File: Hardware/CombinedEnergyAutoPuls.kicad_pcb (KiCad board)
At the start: 2 copper layers, 174.9 x 67 mm, 131 parts, among them J1 Screw_Terminal_01x04, J101 AudioJack3_Switch, J102 Screw_Terminal_01x03, J103 Conn_3P, J2 Screw_Terminal_01x04, J201 Conn_20P_Female, J202 Conn_20P_Female, J203 Conn_4P_Female, J204 Conn_4P_Female, J205 Barrel_Jack_Switch, J3 Pin_Header_1x6, J4 Arduino_USB-Serial_Card_Conne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, J5 Arduino_USB-Serial_Edge_Conne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, J6 AudioJack3_Switch, J7 Screw_Terminal_01x04, Q1 S8550_PNP, Q101 S8050_NPN, Q2 S8050_NPN, Q3 S8050_NPN, SW201 THT_SW_4_Tactile, U1 L78S05CV, U101 LM358DR2G, U102 78L05, U201 PC817, U202 PC817, U203 PC817, U204 PC817, U205 PC817, U206 PC817, U207 PC817, U208 PC817, U209 PC817, U210 PC817, U211 PC817, U212 L78S05CV

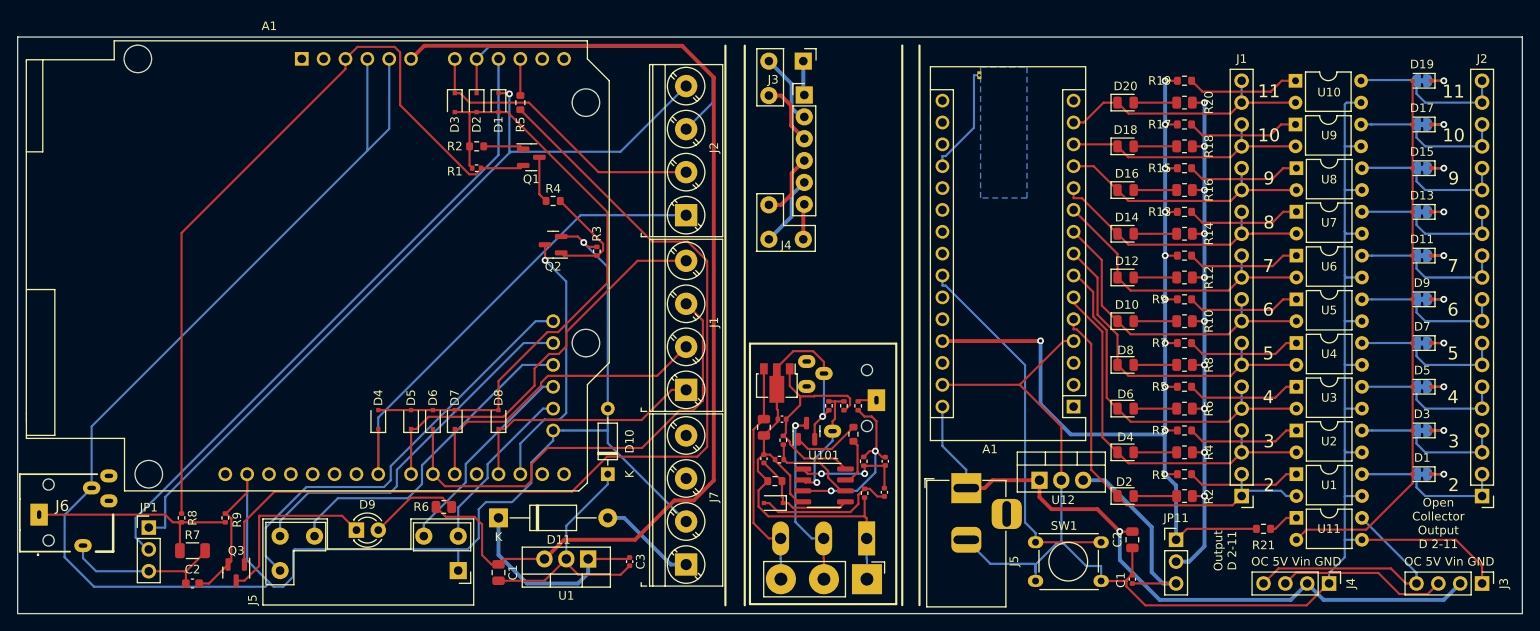
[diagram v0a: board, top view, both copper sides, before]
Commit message: GND zone filled for Energimaaling
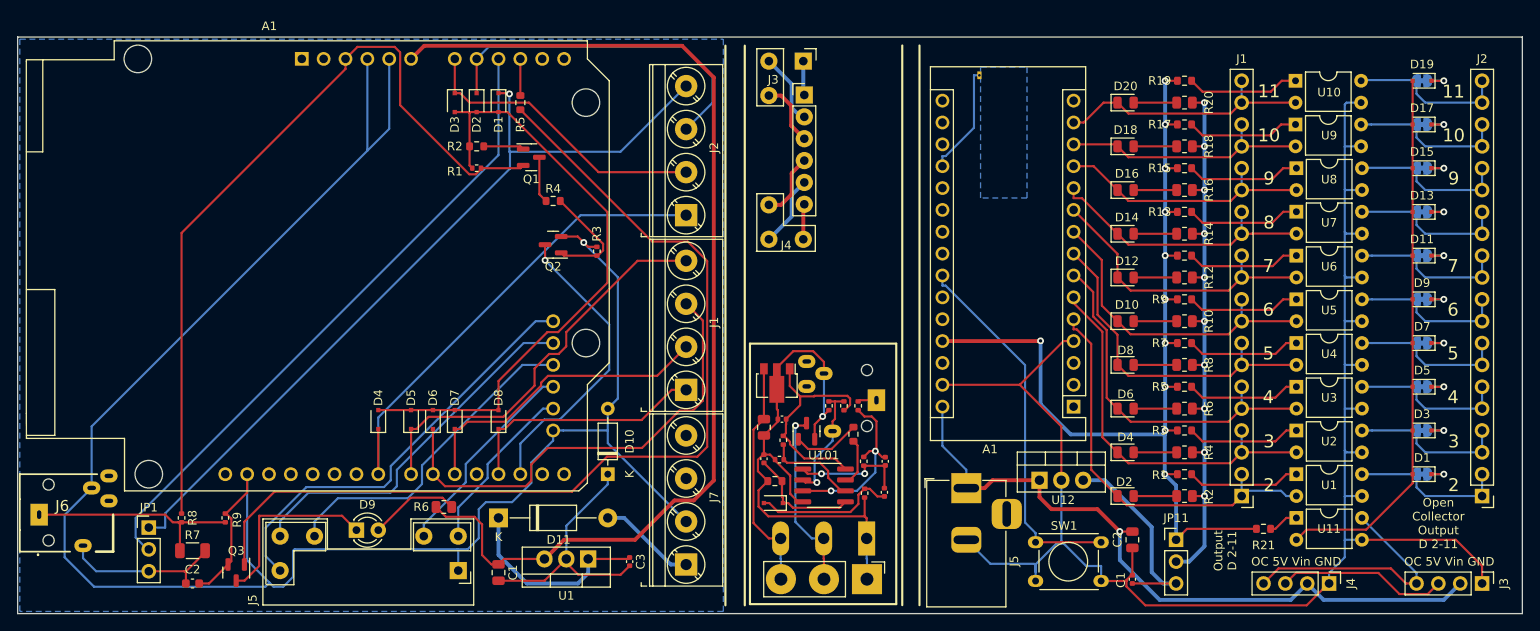
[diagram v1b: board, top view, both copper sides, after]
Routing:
- net Net-(A1-Pad15): track 30.9 -> 35.1 mm
- net GND: track 236.9 -> 237.9 mm
- added copper zone on B.Cu, net GND
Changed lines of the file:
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@@
   (segment (start 8.6 52.4) (end 8.6 45.248) (width 0.25) (layer "B.Cu") (net 4))
   (segment (start 62.23 46.8953) (end 62.23 45.72) (width 0.25) (layer "B.Cu") (net 4))
+  (segment (start 65.786 23.876) (end 65.786 23.9422) (width 0.25) (layer "B.Cu") (net 4))
   (segment (start 68.58 45.72) (end 68.58 47.195) (width 0.25) (layer "B.Cu") (net 4))
   (segment (start 53.5814 58.2433) (end 53.5814 54.8766) (width 0.25) (layer "B.Cu") (net 4))
-  (segment (start 65.786 23.9422) (end 68.58 26.7362) (width 0.25) (layer "B.Cu") (net 4))
-  (segment (start 65.786 23.876) (end 65.786 23.9422) (width 0.25) (layer "B.Cu") (net 4))
+  (segment (start 69.75 42.01) (end 68.58 43.18) (width 0.25) (layer "B.Cu") (net 4))
   (segment (start 28.7834 63.881) (end 29.2622 63.4022) (width 0.25) (layer "B.Cu") (net 4))
   (segment (start 29.741 63.881) (end 29.2622 63.4022) (width 0.25) (layer "B.Cu") (net 4))
-  (segment (start 68.58 26.7362) (end 68.58 43.18) (width 0.25) (layer "B.Cu") (net 4))
   (segment (start 59.69 49.4353) (end 62.23 46.8953) (width 0.25) (layer "B.Cu") (net 4))
   (segment (start 40.7035 13.1445) (end 43.18 10.668) (width 0.25) (layer "B.Cu") (net 4))
@@
   (segment (start 30.861 63.881) (end 29.741 63.881) (width 0.25) (layer "B.Cu") (net 4))
   (segment (start 54.4125 54.0455) (end 57.4605 54.0455) (width 0.25) (layer "B.Cu") (net 4))
+  (segment (start 69.75 27.9062) (end 69.75 42.01) (width 0.25) (layer "B.Cu") (net 4))
   (segment (start 53.5814 54.8766) (end 54.4125 54.0455) (width 0.25) (layer "B.Cu") (net 4))
+  (segment (start 65.786 23.9422) (end 69.75 27.9062) (width 0.25) (layer "B.Cu") (net 4))
   (segment (start 32.004 62.738) (end 30.861 63.881) (width 0.25) (layer "B.Cu") (net 4))
   (segment (start 5.461 55.539) (end 5.461 60.452) (width 0.25) (layer "B.Cu") (net 4))
@@
   (segment (start 61.2925 25.9472) (end 61.2925 24.13) (width 0.25) (layer "F.Cu") (net 14))
   (via (at 61.2925 25.9472) (size 0.8) (drill 0.4) (layers "F.Cu" "B.Cu") (net 14))
+  (segment (start 61.214 44.45) (end 62.992 44.45) (width 0.25) (layer "B.Cu") (net 14))
+  (segment (start 68.75 33.4047) (end 61.2925 25.9472) (width 0.25) (layer "B.Cu") (net 14))
+  (segment (start 68.75 38.692) (end 68.75 33.4047) (width 0.25) (layer "B.Cu") (net 14))
+  (segment (start 62.992 44.45) (end 68.75 38.692) (width 0.25) (layer "B.Cu") (net 14))
   (segment (start 58.42 50.8) (end 58.42 47.244) (width 0.25) (layer "B.Cu") (net 14))
-  (segment (start 62.992 44.45) (end 63.754 43.688) (width 0.25) (layer "B.Cu") (net 14))
-  (segment (start 63.754 28.4087) (end 61.2925 25.9472) (width 0.25) (layer "B.Cu") (net 14))
-  (segment (start 61.214 44.45) (end 62.992 44.45) (width 0.25) (layer "B.Cu") (net 14))
   (segment (start 58.42 47.244) (end 61.214 44.45) (width 0.25) (layer "B.Cu") (net 14))
-  (segment (start 63.754 43.688) (end 63.754 28.4087) (width 0.25) (layer "B.Cu") (net 14))
   (segment (start 77.685 41) (end 76.0097 41) (width 0.25) (layer "F.Cu") (net 15))
   (segment (start 57.664 44.505) (end 72.5047 44.505) (width 0.25) (layer "F.Cu") (net 15))
@@
   (segment (start 55.88 6.52) (end 57.066 6.52) (width 0.25) (layer "F.Cu") (net 35))
   (via (at 57.15 6.604) (size 0.8) (drill 0.4) (layers "F.Cu" "B.Cu") (net 35))
-  (segment (start 17.145 57) (end 17.145 53.467) (width 0.25) (layer "B.Cu") (net 35))
   (segment (start 57.277 13.335) (end 70.05 13.335) (width 0.25) (layer "B.Cu") (net 35))
   (segment (start 15.24 57) (end 17.145 57) (width 0.25) (layer "B.Cu") (net 35))
   (segment (start 57.2135 13.3985) (end 57.277 13.335) (width 0.25) (layer "B.Cu") (net 35))
   (segment (start 70.05 13.335) (end 77.685 5.7) (width 0.25) (layer "B.Cu") (net 35))
-  (segment (start 17.145 53.467) (end 57.2135 13.3985) (width 0.25) (layer "B.Cu") (net 35))
+  (segment (start 57.2135 15.2865) (end 57.2135 13.3985) (width 0.25) (layer "B.Cu") (net 35))
+  (segment (start 17.145 55.355) (end 57.2135 15.2865) (width 0.25) (layer "B.Cu") (net 35))
   (segment (start 57.15 13.335) (end 57.2135 13.3985) (width 0.25) (layer "B.Cu") (net 35))
+  (segment (start 17.145 57) (end 17.145 55.355) (width 0.25) (layer "B.Cu") (net 35))
   (segment (start 57.15 6.604) (end 57.15 13.335) (width 0.25) (layer "B.Cu") (net 35))
   (segment (start 62.81125 34.29) (end 61.55955 34.29) (width 0.25) (layer "F.Cu") (net 36))
@@
       )
     )
+  )
+  (zone (net 4) (net_name "GND") (layer "B.Cu") (hatch edge 0.508)
+    (connect_pads (clearance 0))
+    (min_thickness 0.254) (filled_areas_thickness no)
+    (fill yes (thermal_gap 0.508) (thermal_bridge_width 0.508))
+    (polygon
+      (pts
+        (xy 82 66.75)
+        (xy 0.25 66.75)
+        (xy 0.25 0.25)
+        (xy 82 0.25)
+      )
+    )

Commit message: Feature update - GND zone filled for Arduino USB-Serial card.
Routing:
- added copper zone on B.Cu, net GND3
- added copper zone on F.Cu, net GND3
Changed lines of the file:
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@@
   (segment (start 163.8729 64.7271) (end 165.1 63.5) (width 0.25) (layer "F.Cu") (net 145))
   (segment (start 147.32 63.5) (end 148.5454 62.2746) (width 0.25) (layer "F.Cu") (net 145))
+  (zone (net 68) (net_name "GND3") (layers F&B.Cu) (hatch edge 0.508)
+    (connect_pads (clearance 0))
+    (min_thickness 0.254) (filled_areas_thickness no)
+    (fill yes (thermal_gap 0.508) (thermal_bridge_width 0.508))
+    (polygon
+      (pts
+        (xy 93.25 25.5)
+        (xy 85.25 25.5)
+        (xy 85.25 18)
+        (xy 89.5 18)
+        (xy 89.5 8)
+        (xy 85.25 8)
+        (xy 85.25 1)
+        (xy 93.25 1)
+      )
+    )
+  )
   (zone (net 0) (net_name "") (layers F&B.Cu) (hatch edge 0.508)
     (connect_pads (clearance 0))
